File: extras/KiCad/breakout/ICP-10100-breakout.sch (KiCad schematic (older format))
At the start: 16 parts, among them J1 Conn_01x04, J2 Conn_01x04, J3 Conn_01x04, J4 Conn_01x04, Q1 UM6K34NTCN, U1 ICP-10100, U2 AP7313R

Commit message: reorganized and updated CAD files, added flex probe
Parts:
- C1, C2, C3: footprint Capacitors_SMD:C_0603 -> Capacitor_SMD:C_0603_1608Metric; symbol C_Small -> Device:C_Small
- J1, J2, J3: footprint Pin_Headers:Pin_Header_Straight_1x04_Pitch2.54mm -> Connector_PinHeader_2.54mm:PinHeader_1x04_P2.54mm_Vertical; symbol Conn_01x04 -> Connector_Generic:Conn_01x04
- J4: value Conn_01x04 -> Mouse Bites; symbol Conn_01x04 -> Connector_Generic:Conn_01x04
- L1: footprint Resistors_SMD:R_0603 -> Capacitor_SMD:C_0603_1608Metric; symbol Ferrite_Bead_Small -> Device:Ferrite_Bead_Small
- Q1: footprint TO_SOT_Packages_SMD:SOT-363_SC-70-6 -> Package_TO_SOT_SMD:SOT-363_SC-70-6; symbol FDG1024NZ -> Transistor_FET:FDG1024NZ
- R1, R2, R3, R4, R5: footprint Resistors_SMD:R_0603 -> Resistor_SMD:R_0603_1608Metric; symbol R -> Device:R
- U1: symbol ICP-10100 -> icp-10100:ICP-10100
- U2: footprint TO_SOT_Packages_SMD:SOT-23 -> Package_TO_SOT_SMD:SOT-23; symbol AP1117-18 -> Regulator_Linear:AP1117-18
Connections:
- wire segments 69 -> 86
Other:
- note added: "Bridge\nVDD/SDA/SCL\n1.8V !!"
- note added: "Level-Shifter\nVin to 1.8V"
- note added: "Sensor"
- note added: "VDD/SDA/SCL\nVin = 2.8V to 5V"
- note added: "Voltage Regulator\nVin to 1.8V"

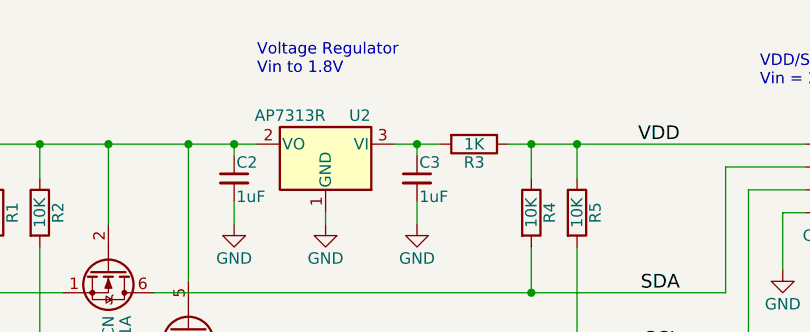
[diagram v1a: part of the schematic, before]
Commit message: add note about reversed footprint of LDO
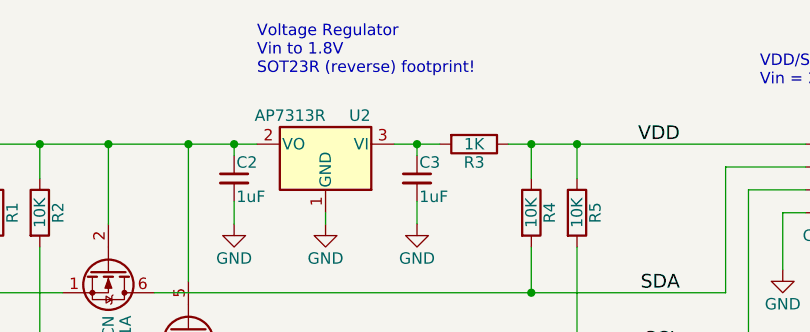
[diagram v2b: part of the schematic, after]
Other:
- note added: "Voltage Regulator\nVin to 1.8V\nSOT23R (reverse) footprint!"
- note removed: "Voltage Regulator\nVin to 1.8V"
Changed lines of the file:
@@
 Bridge\nVDD/SDA/SCL\n1.8V !!
 Text Notes 7000 2500 0    50   ~ 0
-Voltage Regulator\nVin to 1.8V
+Voltage Regulator\nVin to 1.8V\nSOT23R (reverse) footprint!
 Text Notes 6300 4550 0    50   ~ 0
 Level-Shifter\nVin to 1.8V

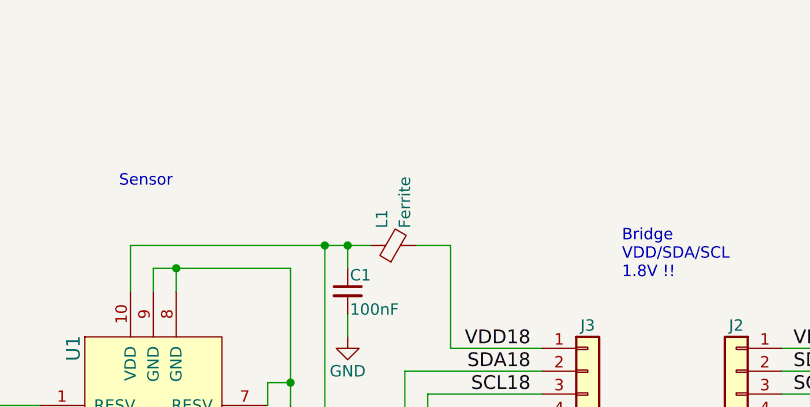
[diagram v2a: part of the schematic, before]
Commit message: add part number for L1, clean-up metadata
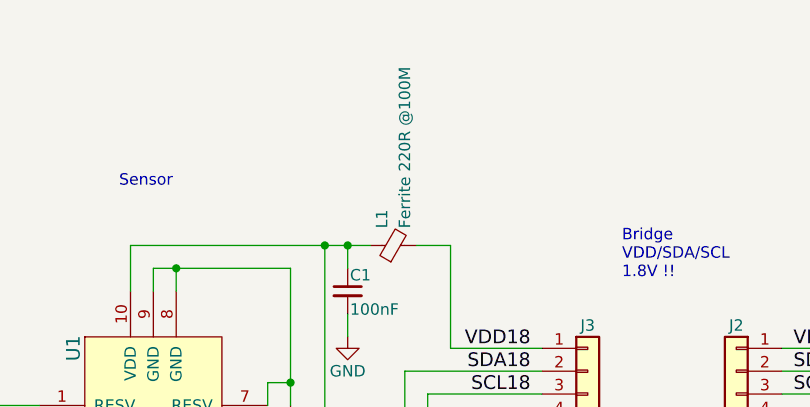
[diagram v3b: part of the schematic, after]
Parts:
- C1, C2, C3, J1, J2, J3, J4, R1, R2, R3, R4, R5: Dist Link Value -> (none); Dist PN Value -> (none)
- L1: value Ferrite -> Ferrite 220R @100M; Dist Link Value -> (none); Dist PN Value -> (none); Mpn (none) -> BLM18PG221SN1D
- Q1: Dist Link Value -> (none); Dist PN Value -> (none); MFG Name ROHM -> (none); MFG Part Num UM6K34NTCN -> (none); Mpn (none) -> UM6K34NTCN
- Q1: Mpn (none) -> UM6K34NTCN
- U1: Dist Link Value -> (none); Dist PN Value -> (none); MFG Name TDK -> (none); MFG Part Num ICP-10100 -> (none); Mpn (none) -> ICP-10100
- U2: footprint Package_TO_SOT_SMD:SOT-23 -> Package_TO_SOT_SMD:SOT-223-3_TabPin2; Dist Link Value -> (none); Dist PN Value -> (none); MFG Name Diodes Inc -> (none); MFG Part Num AP7313-18SRG-7 -> (none); Mpn (none) -> AP7313-18SRG-7
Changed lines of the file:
@@
 F 2 "footprints:ICP-10100" H 2500 3500 60  0001 C CNN
 F 3 "" H 2500 3500 60  0001 C CNN
-F 4 "TDK" H 2500 3500 60  0001 C CNN "MFG Name"
-F 5 "ICP-10100" H 2500 3500 60  0001 C CNN "MFG Part Num"
-F 6 "Value" H 2500 3500 60  0001 C CNN "Dist PN"
-F 7 "Value" H 2500 3500 60  0001 C CNN "Dist Link"
+F 4 "ICP-10100" H 2500 3500 50  0001 C CNN "Mpn"
 	1    2500 3500
 	1    0    0    -1
@@
 F 2 "Capacitor_SMD:C_0603_1608Metric" H 3350 2900 50  0001 C CNN
 F 3 "" H 3350 2900 50  0001 C CNN
-F 4 "Value" H 3350 2900 60  0001 C CNN "Dist PN"
-F 5 "Value" H 3350 2900 60  0001 C CNN "Dist Link"
 	1    3350 2900
 	1    0    0    -1
@@
 F 2 "Package_TO_SOT_SMD:SOT-363_SC-70-6" H 6900 3525 50  0001 L CIN
 F 3 "" H 6700 3600 50  0001 L CNN
+F 4 "UM6K34NTCN" H 6700 3600 50  0001 C CNN "Mpn"
 	2    6700 3600
 	0    1    1    0
@@
 F 2 "Resistor_SMD:R_0603_1608Metric" V 5980 3100 50  0001 C CNN
 F 3 "" H 6050 3100 50  0001 C CNN
-F 4 "Value" H 6050 3100 60  0001 C CNN "Dist PN"
-F 5 "Value" H 6050 3100 60  0001 C CNN "Dist Link"
 	1    6050 3100
 	1    0    0    -1
@@
 F 2 "Resistor_SMD:R_0603_1608Metric" V 5780 3100 50  0001 C CNN
 F 3 "" H 5850 3100 50  0001 C CNN
-F 4 "Value" H 5850 3100 60  0001 C CNN "Dist PN"
-F 5 "Value" H 5850 3100 60  0001 C CNN "Dist Link"
 	1    5850 3100
 	1    0    0    -1
@@
 F 1 "10K" V 8400 3100 50  0000 C CNN
 F 2 "Resistor_SMD:R_0603_1608Metric" V 8330 3100 50  0001 C CNN
-F 3 "~" H 8400 3100 50  0001 C CNN
-F 4 "Value" H 8400 3100 60  0001 C CNN "Dist PN"
-F 5 "Value" H 8400 3100 60  0001 C CNN "Dist Link"
+F 3 "" H 8400 3100 50  0001 C CNN
 	1    8400 3100
 	1    0    0    -1
@@
 F 2 "Resistor_SMD:R_0603_1608Metric" V 8130 3100 50  0001 C CNN
 F 3 "" H 8200 3100 50  0001 C CNN
-F 4 "Value" H 8200 3100 60  0001 C CNN "Dist PN"
-F 5 "Value" H 8200 3100 60  0001 C CNN "Dist Link"
 	1    8200 3100
 	1    0    0    -1
@@
 F 0 "U2" H 7150 2925 50  0000 C CNN
 F 1 "AP7313R" H 7300 2925 50  0000 L CNN
-F 2 "Package_TO_SOT_SMD:SOT-23" H 7300 3000 50  0001 C CNN
+F 2 "Package_TO_SOT_SMD:SOT-223-3_TabPin2" H 7300 3000 50  0001 C CNN
 F 3 "" H 7400 2550 50  0001 C CNN
-F 4 "Diodes Inc" H 7300 2800 60  0001 C CNN "MFG Name"
-F 5 "AP7313-18SRG-7" H 7300 2800 60  0001 C CNN "MFG Part Num"
-F 6 "Value" H 7300 2800 60  0001 C CNN "Dist PN"
-F 7 "Value" H 7300 2800 60  0001 C CNN "Dist Link"
+F 4 "AP7313-18SRG-7" H 7300 2800 50  0001 C CNN "Mpn"
 	1    7300 2800
 	-1   0    0    -1
@@
 F 2 "Capacitor_SMD:C_0603_1608Metric" H 6900 2950 50  0001 C CNN
 F 3 "" H 6900 2950 50  0001 C CNN
-F 4 "Value" H 6900 2950 60  0001 C CNN "Dist PN"
-F 5 "Value" H 6900 2950 60  0001 C CNN "Dist Link"
 	1    6900 2950
 	1    0    0    -1
@@
 F 2 "Capacitor_SMD:C_0603_1608Metric" H 7700 2950 50  0001 C CNN
 F 3 "" H 7700 2950 50  0001 C CNN
-F 4 "Value" H 7700 2950 60  0001 C CNN "Dist PN"
-F 5 "Value" H 7700 2950 60  0001 C CNN "Dist Link"
 	1    7700 2950
 	1    0    0    -1
@@
 F 2 "Resistor_SMD:R_0603_1608Metric" V 7880 2800 50  0001 C CNN
 F 3 "" H 7950 2800 50  0001 C CNN
-F 4 "Value" H 7950 2800 60  0001 C CNN "Dist PN"
-F 5 "Value" H 7950 2800 60  0001 C CNN "Dist Link"
 	1    7950 2800
 	0    1    1    0
@@
 F 2 "Connector_PinHeader_2.54mm:PinHeader_1x04_P2.54mm_Vertical" H 9600 2900 50  0001 C CNN
 F 3 "" H 9600 2900 50  0001 C CNN
-F 4 "Value" H 9600 2900 60  0001 C CNN "Dist PN"
-F 5 "Value" H 9600 2900 60  0001 C CNN "Dist Link"
 	1    9600 2900
 	1    0    0    -1
@@
 P 3550 2700
 F 0 "L1" H 3625 2750 50  0000 L CNN
-F 1 "Ferrite" H 3625 2650 50  0000 L CNN
+F 1 "Ferrite 220R @100M" H 3625 2650 50  0000 L CNN
 F 2 "Capacitor_SMD:C_0603_1608Metric" V 3480 2700 50  0001 C CNN
 F 3 "" H 3550 2700 50  0001 C CNN
-F 4 "Value" H 3550 2700 60  0001 C CNN "Dist PN"
-F 5 "Value" H 3550 2700 60  0001 C CNN "Dist Link"
+F 4 "BLM18PG221SN1D" H 3550 2700 50  0001 C CNN "Mpn"
 	1    3550 2700
 	0    -1   -1   0
@@
 F 2 "Connector_PinHeader_2.54mm:PinHeader_1x04_P2.54mm_Vertical" H 4400 3250 50  0001 C CNN
 F 3 "" H 4400 3250 50  0001 C CNN
-F 4 "Value" H 4400 3250 60  0001 C CNN "Dist PN"
-F 5 "Value" H 4400 3250 60  0001 C CNN "Dist Link"
 	1    4400 3250
 	1    0    0    -1
@@
 F 2 "Connector_PinHeader_2.54mm:PinHeader_1x04_P2.54mm_Vertical" H 5050 3250 50  0001 C CNN
 F 3 "" H 5050 3250 50  0001 C CNN
-F 4 "Value" H 5050 3250 60  0001 C CNN "Dist PN"
-F 5 "Value" H 5050 3250 60  0001 C CNN "Dist Link"
 	1    5050 3250
 	-1   0    0    -1
@@
 F 2 "footprints:Bites" H 4800 4850 50  0001 C CNN
 F 3 "" H 4800 4850 50  0001 C CNN
-F 4 "Value" H 4800 4850 60  0001 C CNN "Dist PN"
-F 5 "Value" H 4800 4850 60  0001 C CNN "Dist Link"
 	1    4800 4850
 	1    0    0    -1
@@
 F 2 "Package_TO_SOT_SMD:SOT-363_SC-70-6" H 6550 3275 50  0001 L CIN
 F 3 "" H 6350 3350 50  0001 L CNN
-F 4 "ROHM" H 6350 3350 60  0001 C CNN "MFG Name"
-F 5 "UM6K34NTCN" H 6350 3350 60  0001 C CNN "MFG Part Num"
-F 6 "Value" H 6350 3350 60  0001 C CNN "Dist PN"
-F 7 "Value" H 6350 3350 60  0001 C CNN "Dist Link"
+F 4 "UM6K34NTCN" H 6350 3350 50  0001 C CNN "Mpn"
 	1    6350 3350
 	0    1    1    0
